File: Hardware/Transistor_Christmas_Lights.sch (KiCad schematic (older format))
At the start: 5 parts, among them Q1 BC848

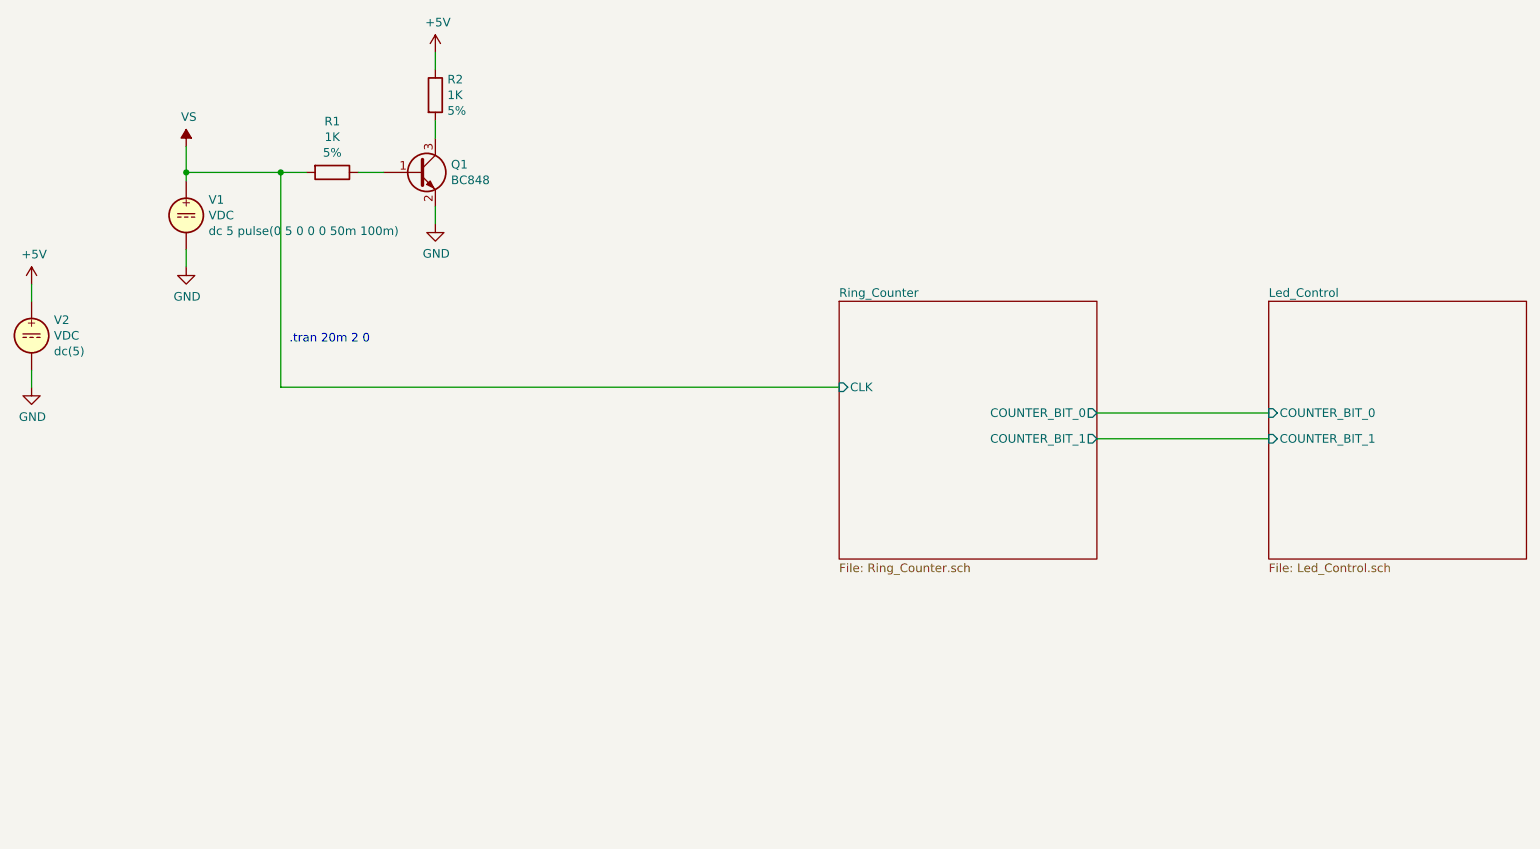
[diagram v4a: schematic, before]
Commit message: Added oscillator to schematic.
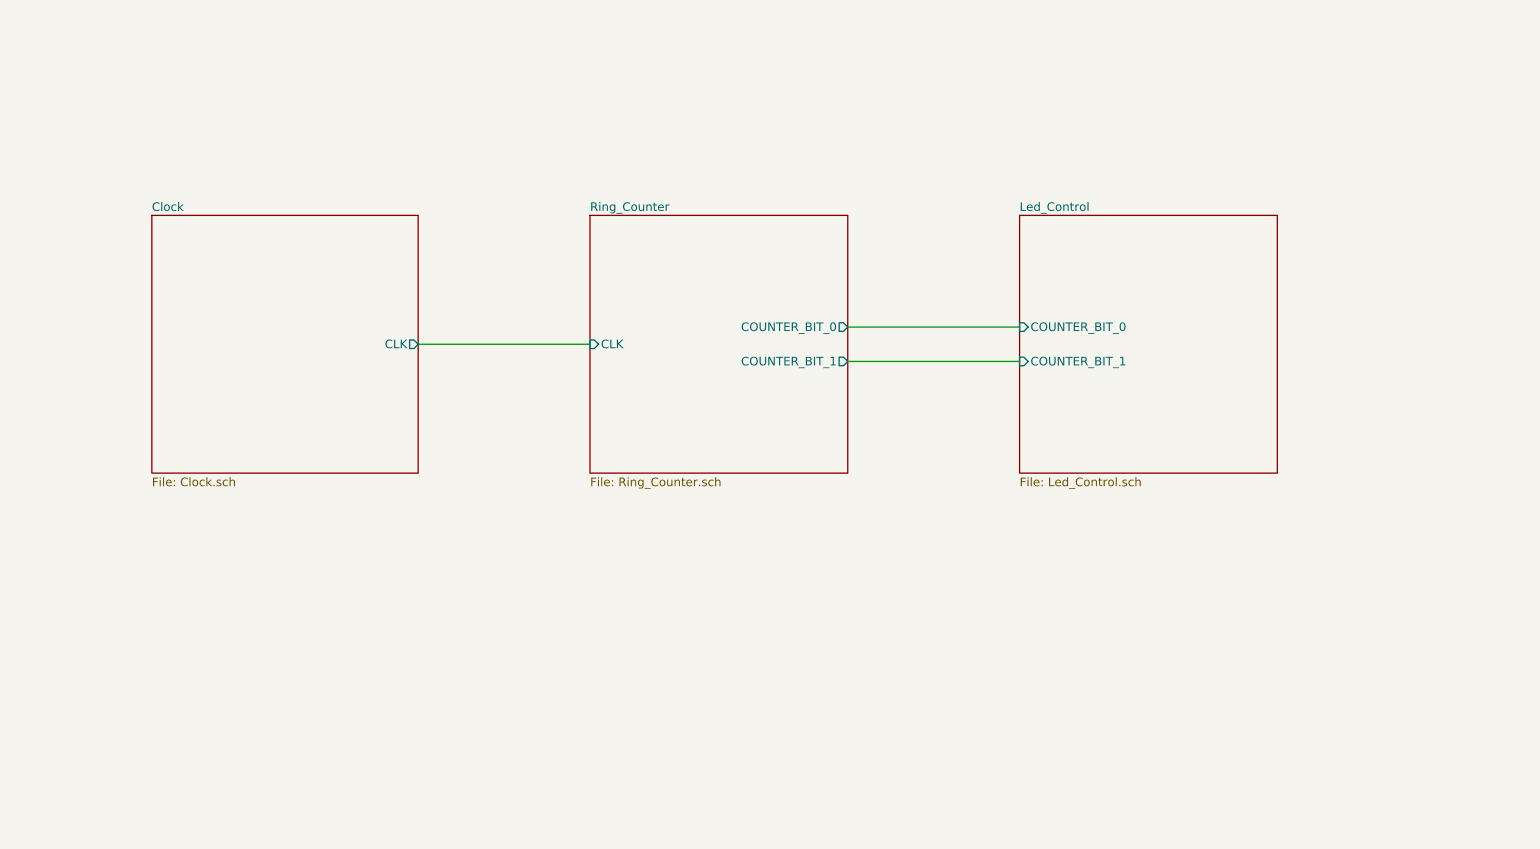
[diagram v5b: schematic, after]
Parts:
- removed Q1: BC848, Package_TO_SOT_SMD:SOT-23, symbol Transistor_BJT:BC848
- removed R1, R2: 1K, Resistor_SMD:R_0603_1608Metric_Pad0.98x0.95mm_HandSolder, symbol Device:R
- removed V1, V2: VDC, symbol Simulation_SPICE:VDC
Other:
- note removed: ".tran 20m 2 0"
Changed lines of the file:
@@
 $Descr A4 11693 8268
 encoding utf-8
-Sheet 1 3
+Sheet 1 4
 Title "Main page"
 Date "2021-12-29"
@@
 Comment4 ""
 $EndDescr
-$Comp
-L Transistor_BJT:BC848 Q1
-U 1 1 61CB54D6
-P 3550 2750
-F 0 "Q1" H 3741 2796 50  0000 L CNN
-F 1 "BC848" H 3741 2705 50  0000 L CNN
-F 2 "Package_TO_SOT_SMD:SOT-23" H 3750 2675 50  0001 L CIN
-F 3 "http://www.infineon.com/dgdl/Infineon-BC847SERIES_BC848SERIES_BC849SERIES_BC850SERIES-DS-v01_01-en.pdf?fileId=db3a304314dca389011541d4630a1657" H 3550 2750 50  0001 L CNN
-F 4 "Q" H 3550 2750 50  0001 C CNN "Spice_Primitive"
-F 5 "BC848" H 3550 2750 50  0001 C CNN "Spice_Model"
-F 6 "Y" H 3550 2750 50  0001 C CNN "Spice_Netlist_Enabled"
-F 7 "Spice_Simulation/BC848.lib" H 3550 2750 50  0001 C CNN "Spice_Lib_File"
-F 8 "3 1 2" H 3550 2750 50  0001 C CNN "Spice_Node_Sequence"
-	1    3550 2750
-	1    0    0    -1
-$EndComp
-$Comp
-L Device:R R2
-U 1 1 61CB5BDA
-P 3650 2300
-F 0 "R2" H 3720 2391 50  0000 L CNN
-F 1 "1K" H 3720 2300 50  0000 L CNN
-F 2 "Resistor_SMD:R_0603_1608Metric_Pad0.98x0.95mm_HandSolder" V 3580 2300 50  0001 C CNN
-F 3 "~" H 3650 2300 50  0001 C CNN
-F 4 "5%" H 3720 2209 50  0000 L CNN "Value2"
-F 5 "R" H 3650 2300 50  0001 C CNN "Spice_Primitive"
-F 6 "1k" H 3650 2300 50  0001 C CNN "Spice_Model"
-F 7 "Y" H 3650 2300 50  0001 C CNN "Spice_Netlist_Enabled"
-	1    3650 2300
-	1    0    0    -1
-$EndComp
-$Comp
-L power:+5V #PWR02
-U 1 1 61CB60D9
-P 3650 2050
-F 0 "#PWR02" H 3650 1900 50  0001 C CNN
-F 1 "+5V" H 3665 2223 50  0000 C CNN
-F 2 "" H 3650 2050 50  0001 C CNN
-F 3 "" H 3650 2050 50  0001 C CNN
-F 4 "V" H 3650 2050 50  0001 C CNN "Spice_Primitive"
-F 5 "dc 5" H 3650 2050 50  0001 C CNN "Spice_Model"
-F 6 "Y" H 3650 2050 50  0001 C CNN "Spice_Netlist_Enabled"
-	1    3650 2050
-	1    0    0    -1
-$EndComp
-$Comp
-L power:GND #PWR03
-U 1 1 61CB63FD
-P 3650 3050
-F 0 "#PWR03" H 3650 2800 50  0001 C CNN
-F 1 "GND" H 3655 2877 50  0000 C CNN
-F 2 "" H 3650 3050 50  0001 C CNN
-F 3 "" H 3650 3050 50  0001 C CNN
-	1    3650 3050
-	1    0    0    -1
-$EndComp
-$Comp
-L Simulation_SPICE:VDC V1
-U 1 1 61CB6CC7
-P 2200 3000
-F 0 "V1" H 2330 3091 50  0000 L CNN
-F 1 "VDC" H 2330 3000 50  0000 L CNN
-F 2 "" H 2200 3000 50  0001 C CNN
-F 3 "~" H 2200 3000 50  0001 C CNN
-F 4 "Y" H 2200 3000 50  0001 L CNN "Spice_Netlist_Enabled"
-F 5 "V" H 2200 3000 50  0001 L CNN "Spice_Primitive"
-F 6 "dc 5 pulse(0 5 0 0 0 50m 100m)" H 2330 2909 50  0000 L CNN "Spice_Model"
-	1    2200 3000
-	1    0    0    -1
-$EndComp
-$Comp
-L power:GND #PWR01
-U 1 1 61CB82BF
-P 2200 3300
-F 0 "#PWR01" H 2200 3050 50  0001 C CNN
-F 1 "GND" H 2205 3127 50  0000 C CNN
-F 2 "" H 2200 3300 50  0001 C CNN
-F 3 "" H 2200 3300 50  0001 C CNN
-	1    2200 3300
-	1    0    0    -1
-$EndComp
-$Comp
-L Device:R R1
-U 1 1 61CB8515
-P 3050 2750
-F 0 "R1" V 2753 2750 50  0000 C CNN
-F 1 "1K" V 2844 2750 50  0000 C CNN
-F 2 "Resistor_SMD:R_0603_1608Metric_Pad0.98x0.95mm_HandSolder" V 2980 2750 50  0001 C CNN
-F 3 "~" H 3050 2750 50  0001 C CNN
-F 4 "5%" V 2935 2750 50  0000 C CNN "Value2"
-F 5 "R" H 3050 2750 50  0001 C CNN "Spice_Primitive"
-F 6 "1k" H 3050 2750 50  0001 C CNN "Spice_Model"
-F 7 "Y" H 3050 2750 50  0001 C CNN "Spice_Netlist_Enabled"
-	1    3050 2750
-	0    1    1    0
-$EndComp
-Wire Wire Line
-	2200 2750 2200 2800
-Wire Wire Line
-	2200 3200 2200 3300
-Text Notes 2800 3750 0    50   ~ 0
-.tran 20m 2 0
-Wire Wire Line
-	3650 2950 3650 3050
-Wire Wire Line
-	3650 2050 3650 2150
-$Comp
-L Simulation_SPICE:VDC V2
-U 1 1 61CC2122
-P 1300 3700
-AR Path="/61CC2122" Ref="V2"  Part="1"
-AR Path="/61CBF5C4/61CC2122" Ref="V?"  Part="1"
-F 0 "V2" H 1430 3791 50  0000 L CNN
-F 1 "VDC" H 1430 3700 50  0000 L CNN
-F 2 "" H 1300 3700 50  0001 C CNN
-F 3 "~" H 1300 3700 50  0001 C CNN
-F 4 "Y" H 1300 3700 50  0001 L CNN "Spice_Netlist_Enabled"
-F 5 "V" H 1300 3700 50  0001 L CNN "Spice_Primitive"
-F 6 "dc(5)" H 1430 3609 50  0000 L CNN "Spice_Model"
-	1    1300 3700
-	1    0    0    -1
-$EndComp
-$Comp
-L power:GND #PWR05
-U 1 1 61CC2128
-P 1300 4000
-AR Path="/61CC2128" Ref="#PWR05"  Part="1"
-AR Path="/61CBF5C4/61CC2128" Ref="#PWR?"  Part="1"
-F 0 "#PWR05" H 1300 3750 50  0001 C CNN
-F 1 "GND" H 1305 3827 50  0000 C CNN
-F 2 "" H 1300 4000 50  0001 C CNN
-F 3 "" H 1300 4000 50  0001 C CNN
-	1    1300 4000
-	1    0    0    -1
-$EndComp
-$Comp
-L power:+5V #PWR04
-U 1 1 61CC2131
-P 1300 3400
-F 0 "#PWR04" H 1300 3250 50  0001 C CNN
-F 1 "+5V" H 1315 3573 50  0000 C CNN
-F 2 "" H 1300 3400 50  0001 C CNN
-F 3 "" H 1300 3400 50  0001 C CNN
-F 4 "V" H 1300 3400 50  0001 C CNN "Spice_Primitive"
-F 5 "dc 5" H 1300 3400 50  0001 C CNN "Spice_Model"
-F 6 "Y" H 1300 3400 50  0001 C CNN "Spice_Netlist_Enabled"
-	1    1300 3400
-	1    0    0    -1
-$EndComp
-Wire Wire Line
-	1300 3400 1300 3500
-Wire Wire Line
-	1300 3900 1300 4000
-Wire Wire Line
-	3200 2750 3350 2750
-Wire Wire Line
-	3650 2450 3650 2550
-Wire Wire Line
-	2200 2750 2750 2750
 $Sheet
-S 8500 3500 1500 1500
+S 7050 3000 1500 1500
 U 61CE6682
 F0 "Led_Control" 50
 F1 "Led_Control.sch" 50
-F2 "COUNTER_BIT_0" I L 8500 4150 50
-F3 "COUNTER_BIT_1" I L 8500 4300 50
+F2 "COUNTER_BIT_0" I L 7050 3650 50
+F3 "COUNTER_BIT_1" I L 7050 3850 50
 $EndSheet
-Wire Wire Line
-	2200 2600 2200 2750
-Connection ~ 2200 2750
-$Comp
-L power:VS #PWR06
-U 1 1 61CE7722
-P 2200 2600
-F 0 "#PWR06" H 2000 2450 50  0001 C CNN
-F 1 "VS" H 2215 2773 50  0000 C CNN
-F 2 "" H 2200 2600 50  0001 C CNN
-F 3 "" H 2200 2600 50  0001 C CNN
-	1    2200 2600
-	1    0    0    -1
-$EndComp
 $Sheet
-S 6000 3500 1500 1500
+S 4550 3000 1500 1500
 U 61D90E9A
 F0 "Ring_Counter" 50
 F1 "Ring_Counter.sch" 50
-F2 "COUNTER_BIT_0" O R 7500 4150 50
-F3 "COUNTER_BIT_1" O R 7500 4300 50
-F4 "CLK" I L 6000 4000 50
+F2 "COUNTER_BIT_0" O R 6050 3650 50
+F3 "COUNTER_BIT_1" O R 6050 3850 50
+F4 "CLK" I L 4550 3750 50
 $EndSheet
 Wire Wire Line
-	7500 4150 8500 4150
+	6050 3650 7050 3650
 Wire Wire Line
-	8500 4300 7500 4300
+	7050 3850 6050 3850
+$Sheet
+S 2000 3000 1550 1500
+U 622B55AD
+F0 "Clock" 50
+F1 "Clock.sch" 50
+F2 "CLK" O R 3550 3750 50
+$EndSheet
 Wire Wire Line
-	2750 2750 2750 4000
-Wire Wire Line
-	2750 4000 6000 4000
-Connection ~ 2750 2750
-Wire Wire Line
-	2750 2750 2900 2750
+	3550 3750 4550 3750
 $EndSCHEMATC
